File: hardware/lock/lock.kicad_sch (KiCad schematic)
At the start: 0 parts

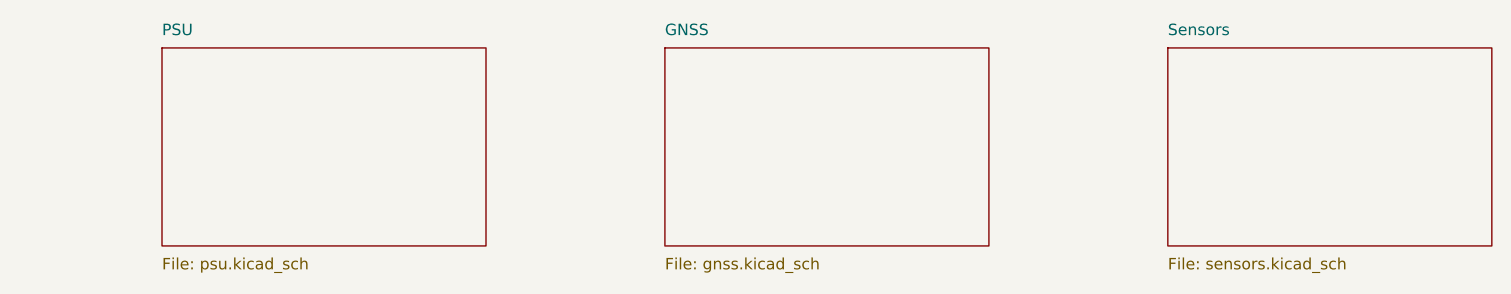
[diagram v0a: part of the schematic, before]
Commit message: lock: add companion TOTP lock board + authenticated lock interface
Add hardware/lock — a second PCB in this repo (shares scripts/kschgen.py,
Makefile, and lib tables, like reefvolt-sensorbuddy):
- ATtiny1616 controller running directly off the 1S cell (no LDO, ~0.1uA
  power-down), a gated MT3608 boost to 12V with a reservoir cap, and an
  AO3400A + SS34 low-side peak-and-hold solenoid driver. All-JLCPCB BOM.
- Authenticated digital link to ephemerkey: 4-wire UART + firmware
  HMAC-SHA1 challenge-response (reuses smalltotp; nonce anti-replay;
  pairing secret in flash). UPDI programming header (J4).
- Sheets are placed-not-wired; on-canvas notes carry the wiring spec.

ephemerkey side:
- Rework J2 from the one-way LOCK_OUT strobe to the matching authenticated
  UART (KEY_TX/KEY_RX + CODE_REQ wake on PB3).
- DESIGN.md: authenticated interface contract + firmware plan; pin table.
- Regenerate sheets (manifest-driven; regen reassigns UUIDs).

hardware/Makefile: add `lock` to PROJECTS.

Co-Authored-By: Claude Opus 4.8 (1M context) <noreply@anthropic.com>
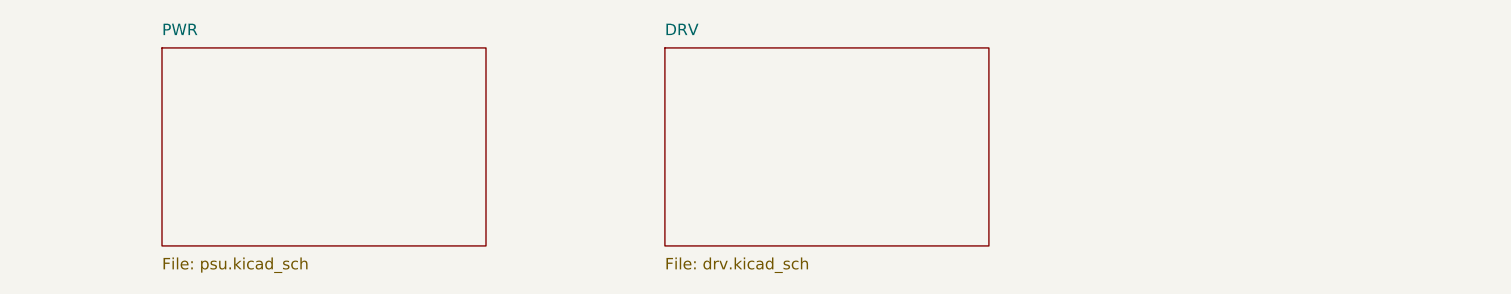
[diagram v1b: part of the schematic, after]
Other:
- removed sheet GNSS
- removed sheet PSU
- removed sheet Sensors
- added sheet DRV (drv.kicad_sch)
- added sheet PWR (psu.kicad_sch)
- title: ephemerkey -> lock
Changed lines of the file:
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@@
 	(paper "A3")
 	(title_block
-		(title "ephemerkey")
-		(date "2026-06-21")
+		(title "lock")
+		(date "2026-06-28")
 		(rev "0.1")
 		(company "EphemerKey Authors")
-		(comment 1 "GPS-geofenced TOTP (RFC 6238) generator")
-		(comment 2 "Top-level — hierarchical sheets per subsystem")
+		(comment 1 "Companion TOTP lock — authenticated 12V solenoid driver")
+		(comment 2 "ATtiny1616 (firmware HMAC); 1S Li-ion; peak-and-hold economizer")
 	)
 	(sheet
@@
 		(stroke (width 0.1524) (type solid))
 		(fill (color 0 0 0 0.0000))
-		(property "Sheetname" "PSU"
+		(property "Sheetname" "PWR"
 			(at 96.52 39.37 0)
 			(effects (font (size 1.27 1.27)) (justify left bottom))
@@
 		(stroke (width 0.1524) (type solid))
 		(fill (color 0 0 0 0.0000))
-		(property "Sheetname" "GNSS"
+		(property "Sheetname" "DRV"
 			(at 152.40 39.37 0)
 			(effects (font (size 1.27 1.27)) (justify left bottom))
 		)
-		(property "Sheetfile" "gnss.kicad_sch"
+		(property "Sheetfile" "drv.kicad_sch"
 			(at 152.40 63.91 0)
 			(effects (font (size 1.27 1.27)) (justify left top))
 		)
-	)
-	(sheet
-		(at 208.28 40.64)
-		(size 36.00 22.00)
-		(fields_autoplaced yes)
-		(stroke (width 0.1524) (type solid))
-		(fill (color 0 0 0 0.0000))
-		(property "Sheetname" "Sensors"
-			(at 208.28 39.37 0)
-			(effects (font (size 1.27 1.27)) (justify left bottom))
-		)
-		(property "Sheetfile" "sensors.kicad_sch"
-			(at 208.28 63.91 0)
-			(effects (font (size 1.27 1.27)) (justify left top))
-		)

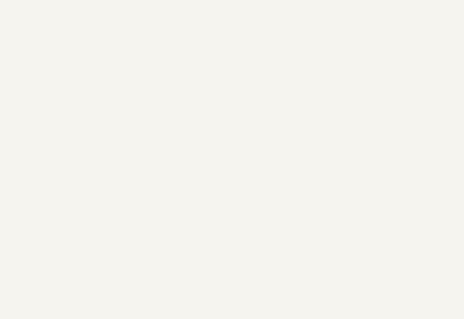
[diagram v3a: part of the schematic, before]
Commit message: lock: second servo output, clearer wiring notes, start PCB layout
- Add a second servo output (J8 + SERVO_SIG2 on PB4, R24/R25) sharing the
  VSERVO rail and the load-switch/interlock -- e.g. a dual-latch lock.
- Rewrite the per-sheet wiring notes (MCU/PWR/DRV) from prose into terse
  pin -> net maps: one line per part, every pin = its net, with a NETS IN
  header for cross-sheet signals. Rationale stays in the README.
- kschgen: park the wiring note below all placed components so the text no
  longer overlaps symbols (computed from the last component row).
- Start the lock PCB layout (hardware/lock/lock.kicad_pcb).

Board regenerates + checks clean (49 components; all footprints carry 3D models).

Co-Authored-By: Claude Opus 4.8 (1M context) <noreply@anthropic.com>
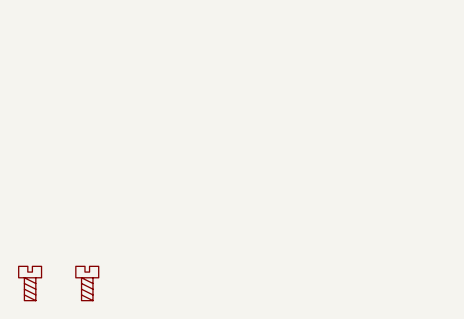
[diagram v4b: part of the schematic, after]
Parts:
- added H2, H3: MountingScrew, MountingHole:MountingHole_3.2mm_M3_Pad_TopBottom, symbol Auxiliary_Items:MountingScrew
